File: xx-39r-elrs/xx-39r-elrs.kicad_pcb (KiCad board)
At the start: 2 copper layers, 35 x 44 mm, 47 parts, among them J1 SENSE, J10 PA2, J11 PWR1, J12 PWR2, J13 R_VCC, J14 GND1, J15 GND2, J16 GND3, J2 BAT, J3 M_PORT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

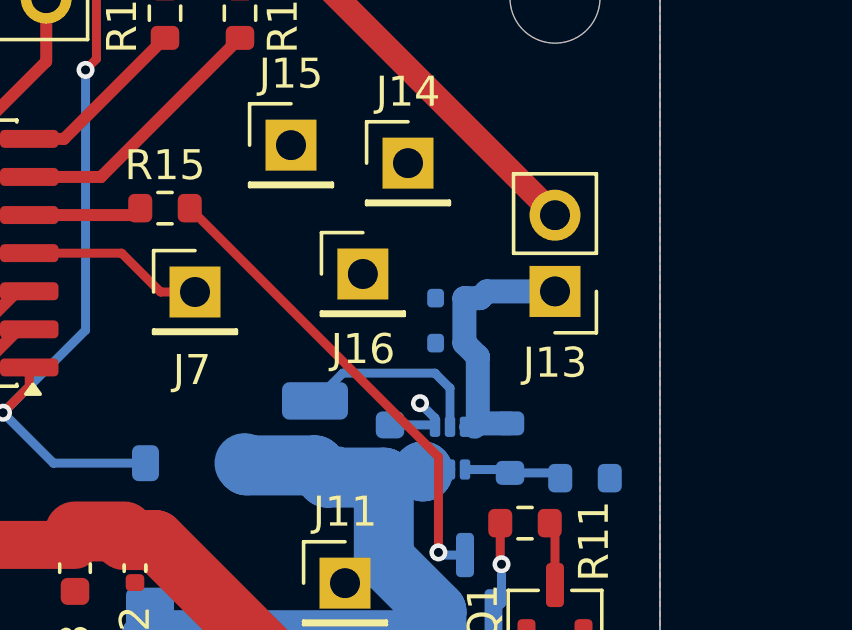
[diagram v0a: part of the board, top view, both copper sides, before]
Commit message: Use 0805 for C21/C22
The actual capacitance of the old 0402 might drop below TPS
requirements under load.
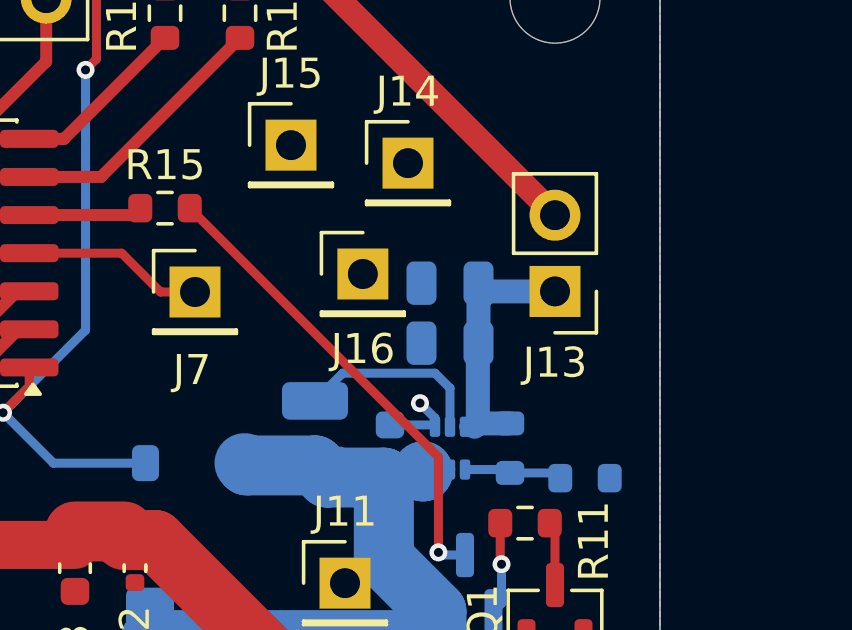
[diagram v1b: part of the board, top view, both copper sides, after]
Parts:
- C21, C22: footprint Capacitor_SMD:C_0402_1005Metric -> Capacitor_SMD:C_0805_2012Metric
- moved C22 0.50 mm to (85.5, 52.5)
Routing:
- net Net-(J13-Pin_1): track 9.02 -> 7.87 mm
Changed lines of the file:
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@@
 			)
 		)
-		(property "KiLib_Generator" "connector/pin_header_socket"
-			(at 0 0 0)
-			(layer "F.SilkS")
-			(hide yes)
-			(effects
-				(font
-					(size 1 1)
-					(thickness 0.15)
-				)
-			)
-		)
 		(property ki_fp_filters "Connector*:*_1x??_*")
 		(sheetname "/")
@@
 			)
 		)
-		(property "KiLib_Generator" "connector/pin_header_socket"
-			(at 0 0 0)
-			(layer "F.SilkS")
-			(hide yes)
-			(effects
-				(font
-					(size 1 1)
-					(thickness 0.15)
-				)
-			)
-		)
 		(property ki_fp_filters "Connector*:*_1x??_*")
 		(sheetname "/")
@@
 			)
 		)
-		(property "KiLib_Generator" "connector/pin_header_socket"
-			(at 0 0 0)
-			(layer "F.SilkS")
-			(hide yes)
-			(effects
-				(font
-					(size 1 1)
-					(thickness 0.15)
-				)
-			)
-		)
 		(property ki_fp_filters "Connector*:*_1x??_*")
 		(sheetname "/")
@@
 		)
 	)
-	(footprint "Capacitor_SMD:C_0402_1005Metric"
+	(footprint "Capacitor_SMD:C_0805_2012Metric"
 		(layer "B.Cu")
-		(at 85.5 53)
-		(descr "Capacitor SMD 0402 (1005 Metric), square (rectangular) end terminal, IPC-7351 nominal, (Body size source: IPC-SM-782 page 76, https://www.pcb-3d.com/wordpress/wp-content/uploads/ipc-sm-782a_amendment_1_and_2.pdf)")
+		(at 85.5 52.5)
+		(descr "Capacitor SMD 0805 (2012 Metric), square (rectangular) end terminal, IPC-7351 nominal, (Body size source: IPC-SM-782 page 76, https://www.pcb-3d.com/wordpress/wp-content/uploads/ipc-sm-782a_amendment_1_and_2.pdf, https://docs.google.com/spreadsheets/d/1BsfQQcO9C6DZCsRaXUlFlo91Tg2WpOkGARC1WS5S8t0/edit?usp=sharing)")
 		(tags "capacitor")
 		(property "Reference" "C22"
-			(at -0.4 -1.2 0)
+			(at 0 1.68 180)
 			(layer "B.SilkS")
 			(effects
@@
 		)
 		(property "Value" "22uF"
-			(at 0 -1.16 0)
+			(at 0 -1.68 180)
 			(layer "B.Fab")
 			(effects
@@
 		)
 		(property "Datasheet" ""
-			(at 0 0 0)
+			(at 0 0 180)
 			(layer "B.Fab")
 			(hide yes)
@@
 		)
 		(property "Description" "Unpolarized capacitor"
-			(at 0 0 0)
+			(at 0 0 180)
 			(layer "B.Fab")
 			(hide yes)
@@
 		(duplicate_pad_numbers_are_jumpers no)
 		(fp_line
-			(start -0.107836 -0.36)
-			(end 0.107836 -0.36)
+			(start -0.261252 -0.735)
+			(end 0.261252 -0.735)
 			(stroke
 				(width 0.12)
@@
 		)
 		(fp_line
-			(start -0.107836 0.36)
-			(end 0.107836 0.36)
+			(start -0.261252 0.735)
+			(end 0.261252 0.735)
 			(stroke
 				(width 0.12)
@@
 		)
 		(fp_rect
-			(start -0.91 0.46)
-			(end 0.91 -0.46)
+			(start -1.7 0.98)
+			(end 1.7 -0.98)
 			(stroke
 				(width 0.05)
@@
 		)
 		(fp_rect
-			(start -0.5 0.25)
-			(end 0.5 -0.25)
+			(start -1 0.625)
+			(end 1 -0.625)
 			(stroke
 				(width 0.1)
@@
 		)
 		(fp_text user "${REFERENCE}"
-			(at 0 0 0)
+			(at 0 0 180)
 			(layer "B.Fab")
 			(effects
 				(font
-					(size 0.25 0.25)
-					(thickness 0.04)
+					(size 0.5 0.5)
+					(thickness 0.08)
 				)
 				(justify mirror)
@@
 		)
 		(pad "1" smd roundrect
-			(at -0.48 0)
-			(size 0.56 0.62)
+			(at -0.95 0)
+			(size 1 1.45)
 			(layers "B.Cu" "B.Mask" "B.Paste")
 			(roundrect_rratio 0.25)
@@
 		)
 		(pad "2" smd roundrect
-			(at 0.48 0)
-			(size 0.56 0.62)
+			(at 0.95 0)
+			(size 1 1.45)
 			(layers "B.Cu" "B.Mask" "B.Paste")
 			(roundrect_rratio 0.25)
@@
 		)
 		(embedded_fonts no)
-		(model "${KICAD10_3DMODEL_DIR}/Capacitor_SMD.3dshapes/C_0402_1005Metric.step"
+		(model "${KICAD10_3DMODEL_DIR}/Capacitor_SMD.3dshapes/C_0805_2012Metric.step"
 			(offset
 				(xyz 0 0 0)
@@
 		)
 	)
-	(footprint "Capacitor_SMD:C_0402_1005Metric"
+	(footprint "Capacitor_SMD:C_0805_2012Metric"
 		(layer "B.Cu")
 		(at 85.5 54.5)
-		(descr "Capacitor SMD 0402 (1005 Metric), square (rectangular) end terminal, IPC-7351 nominal, (Body size source: IPC-SM-782 page 76, https://www.pcb-3d.com/wordpress/wp-content/uploads/ipc-sm-782a_amendment_1_and_2.pdf)")
+		(descr "Capacitor SMD 0805 (2012 Metric), square (rectangular) end terminal, IPC-7351 nominal, (Body size source: IPC-SM-782 page 76, https://www.pcb-3d.com/wordpress/wp-content/uploads/ipc-sm-782a_amendment_1_and_2.pdf, https://docs.google.com/spreadsheets/d/1BsfQQcO9C6DZCsRaXUlFlo91Tg2WpOkGARC1WS5S8t0/edit?usp=sharing)")
 		(tags "capacitor")
 		(property "Reference" "C21"
-			(at 0 1.16 0)
+			(at 0 1.68 180)
 			(layer "B.SilkS")
 			(effects
@@
 		)
 		(property "Value" "22uF"
-			(at 0 -1.16 0)
+			(at 0 -1.68 180)
 			(layer "B.Fab")
 			(effects
@@
 		)
 		(property "Datasheet" ""
-			(at 0 0 0)
+			(at 0 0 180)
 			(layer "B.Fab")
 			(hide yes)
@@
 		)
 		(property "Description" "Unpolarized capacitor"
-			(at 0 0 0)
+			(at 0 0 180)
 			(layer "B.Fab")
 			(hide yes)
@@
 		(duplicate_pad_numbers_are_jumpers no)
 		(fp_line
-			(start -0.107836 -0.36)
-			(end 0.107836 -0.36)
+			(start -0.261252 -0.735)
+			(end 0.261252 -0.735)
 			(stroke
 				(width 0.12)
@@
 		)
 		(fp_line
-			(start -0.107836 0.36)
-			(end 0.107836 0.36)
+			(start -0.261252 0.735)
+			(end 0.261252 0.735)
 			(stroke
 				(width 0.12)
@@
 		)
 		(fp_rect
-			(start -0.91 0.46)
-			(end 0.91 -0.46)
+			(start -1.7 0.98)
+			(end 1.7 -0.98)
 			(stroke
 				(width 0.05)
@@
 		)
 		(fp_rect
-			(start -0.5 0.25)
-			(end 0.5 -0.25)
+			(start -1 0.625)
+			(end 1 -0.625)
 			(stroke
 				(width 0.1)
@@
 		)
 		(fp_text user "${REFERENCE}"
-			(at 0 0 0)
+			(at 0 0 180)
 			(layer "B.Fab")
 			(effects
 				(font
-					(size 0.25 0.25)
-					(thickness 0.04)
+					(size 0.5 0.5)
+					(thickness 0.08)
 				)
 				(justify mirror)
@@
 		)
 		(pad "1" smd roundrect
-			(at -0.48 0)
-			(size 0.56 0.62)
+			(at -0.95 0)
+			(size 1 1.45)
 			(layers "B.Cu" "B.Mask" "B.Paste")
 			(roundrect_rratio 0.25)
@@
 		)
 		(pad "2" smd roundrect
-			(at 0.48 0)
-			(size 0.56 0.62)
+			(at 0.95 0)
+			(size 1 1.45)
 			(layers "B.Cu" "B.Mask" "B.Paste")
 			(roundrect_rratio 0.25)
@@
 		)
 		(embedded_fonts no)
-		(model "${KICAD10_3DMODEL_DIR}/Capacitor_SMD.3dshapes/C_0402_1005Metric.step"
+		(model "${KICAD10_3DMODEL_DIR}/Capacitor_SMD.3dshapes/C_0805_2012Metric.step"
 			(offset
 				(xyz 0 0 0)
@@
 	)
 	(segment
-		(start 85.98 54.5)
-		(end 85.98 53)
-		(width 0.8)
-		(layer "B.Cu")
-		(net "Net-(J13-Pin_1)")
-	)
-	(segment
 		(start 86.5 53)
 		(end 86.725 52.775)
@@
 	)
 	(segment
-		(start 86.428 57.175)
-		(end 87.5 57.175)
-		(width 0.8)
-		(layer "B.Cu")
-		(net "Net-(J13-Pin_1)")
-	)
-	(segment
-		(start 86.428 54.948)
-		(end 85.98 54.5)
+		(start 86.45 53)
+		(end 86.45 54.5)
 		(width 0.8)
 		(layer "B.Cu")
@@
 	)
 	(segment
-		(start 85.98 53)
-		(end 86.5 53)
+		(start 86.428 57.175)
+		(end 87.5 57.175)
 		(width 0.8)
 		(layer "B.Cu")
